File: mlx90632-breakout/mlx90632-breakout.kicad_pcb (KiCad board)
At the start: 2 copper layers, 7.6 x 19 mm, 7 parts, among them J1 Conn_01x04_Male, U1 MLX90632SLD-BCB-000-SP

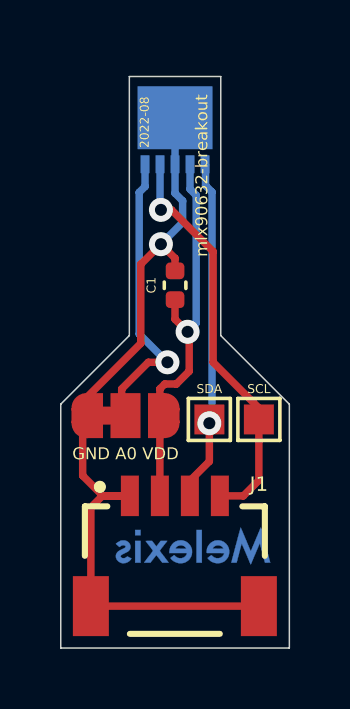
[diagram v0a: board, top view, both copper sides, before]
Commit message: updated breakout boards
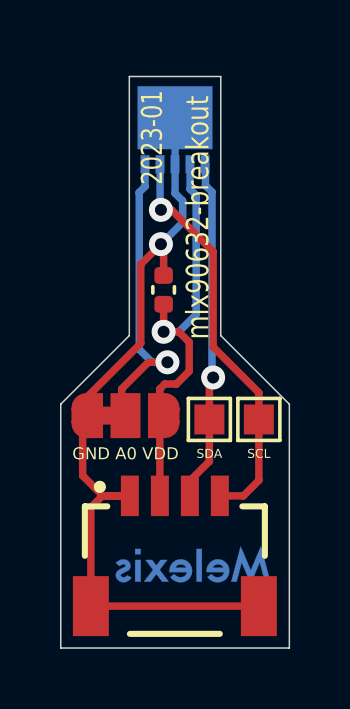
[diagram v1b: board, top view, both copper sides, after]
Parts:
- moved G*** 0.64 mm to (110.9, 80.7)
- moved C1 0.41 mm to (110.6, 71.6)
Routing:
- net /VDD: track 13.2 -> 14.1 mm
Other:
- board text added: "2023-01"
- board text added: "MLX90632"
- board text removed: "2022-08"
